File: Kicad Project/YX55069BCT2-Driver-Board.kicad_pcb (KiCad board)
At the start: 6 copper layers, 54.3 x 33.2 mm, 151 parts, among them J1 10029449-001RLF, Q1 BSS138_C112239, Q2 BSS138_C112239, Q4 BSS138_C112239, SW3 BOOT, SW4 RESET, U1 TC358870XBG(NOK), U10 ESP32-S3R8, U11 GD25Q128EWIGR, U12 USBLC6-2SC6, U13 SN74AXC1T45DCKR, U14 TXS0101DBVR, U15 TPS61165DBVR, U16 TVS0500DRVR, U2 TLV76701DRVR, U3 CH224K, U4 TLV76718DRVR, U5 TLV76728DRVR, U6 TLV76733DRVR, U62 PCA9306DCUR, U63 AP2120N-2.8TRG1, U64 PCA9306DCUR, U7 TLV76701DRVR, U8 ESD7104MUTAG_C2987068, U9 TPS259474LRPWR, X1 ABM8-40.000MHZ-10-D1G-T

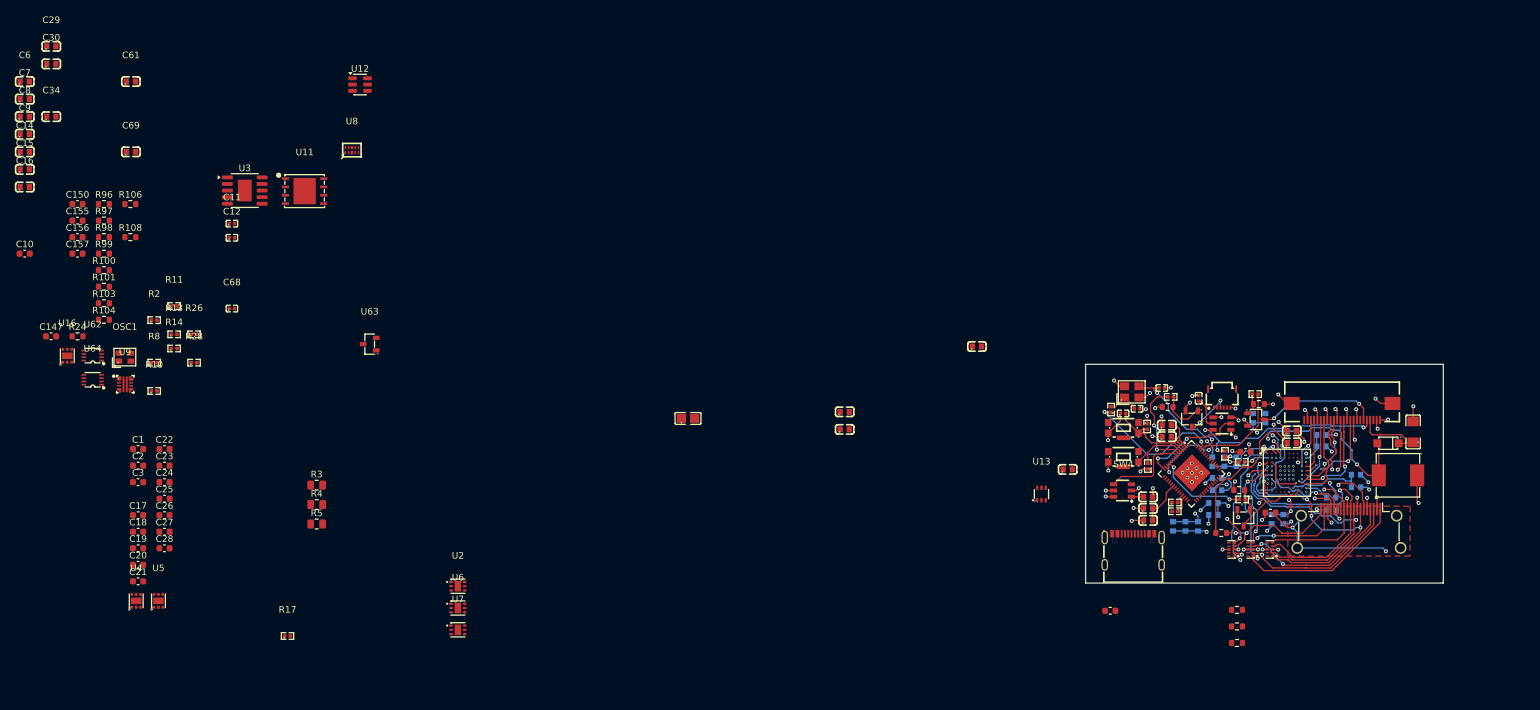
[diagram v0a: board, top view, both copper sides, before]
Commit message: wired up LDOs + USB-C
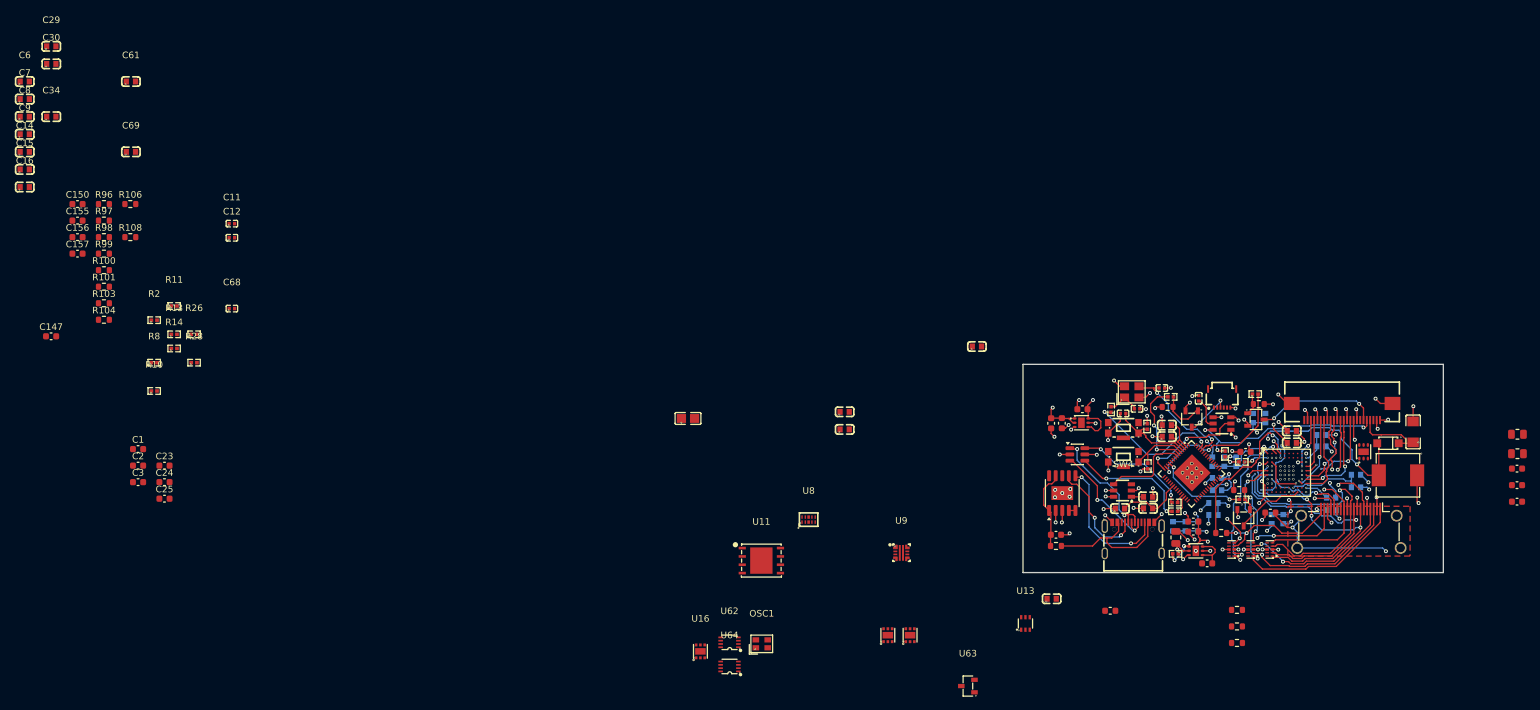
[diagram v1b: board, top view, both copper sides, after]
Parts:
- moved C17 209.5 mm to (163.8, 74.2)
- moved C18 209.5 mm to (163.8, 76.7)
- moved C19 209.5 mm to (163.8, 79.2)
- moved R3 182.5 mm to (163.9, 69.0)
- moved R4 182.5 mm to (163.9, 71.9)
- moved C10 162.3 mm to (93.8, 84.2)
- moved C28 158.3 mm to (116.8, 88.5), turned to 180 degrees
- moved C26 156.2 mm to (114.7, 82.2)
- moved C27 156.2 mm to (114.7, 83.7)
- moved R24 151.9 mm to (93.8, 85.9)
- moved C21 142.3 mm to (94.7, 67.3), turned to 90 degrees
- moved C20 140.3 mm to (93.1, 67.3), turned to 90 degrees
- moved C22 139.5 mm to (97.8, 65.2), turned to 180 degrees
- moved U2 139.0 mm to (140.5, 71.6), turned to 90 degrees
- moved R17 135.4 mm to (111.9, 87.1), turned to 180 degrees
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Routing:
- net GND: track 103.9 -> 126.0 mm, vias 81 -> 102
- net VBUS: track 0.00 -> 21.2 mm
- net CC2: track 0.00 -> 21.0 mm, vias 0 -> 2
- net USB_DN: track 0.00 -> 18.7 mm, vias 0 -> 2
- net USB_DP: track 0.00 -> 18.4 mm, vias 0 -> 2
- net ESP_DP: track 0.00 -> 18.0 mm, vias 0 -> 2
- net ESP_DN: track 0.00 -> 17.6 mm, vias 0 -> 2
- net CC1: track 0.00 -> 16.9 mm, vias 0 -> 2
- net SYS_5V: track 9.35 -> 25.6 mm, vias 3 -> 5
- net VDD: track 0.00 -> 12.2 mm
- net 1V15: track 35.4 -> 46.6 mm, vias 11 -> 14
- net Net-(U7-FB): track 0.00 -> 9.84 mm, vias 0 -> 2
- net 3V3: track 63.7 -> 73.4 mm, vias 11 -> 12
- net Net-(U3-DM): track 0.00 -> 1.00 mm
- added copper zone on In6.Cu, net 1V15
- added copper zone on In5.Cu, net 3V3
- added copper zone on In3.Cu, net GND
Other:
- board size 54.3 x 33.2 mm -> 63.8 x 31.6 mm
- copper layers 6 -> 8

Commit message: wired rest of components, and majority of remaining caps and resistors
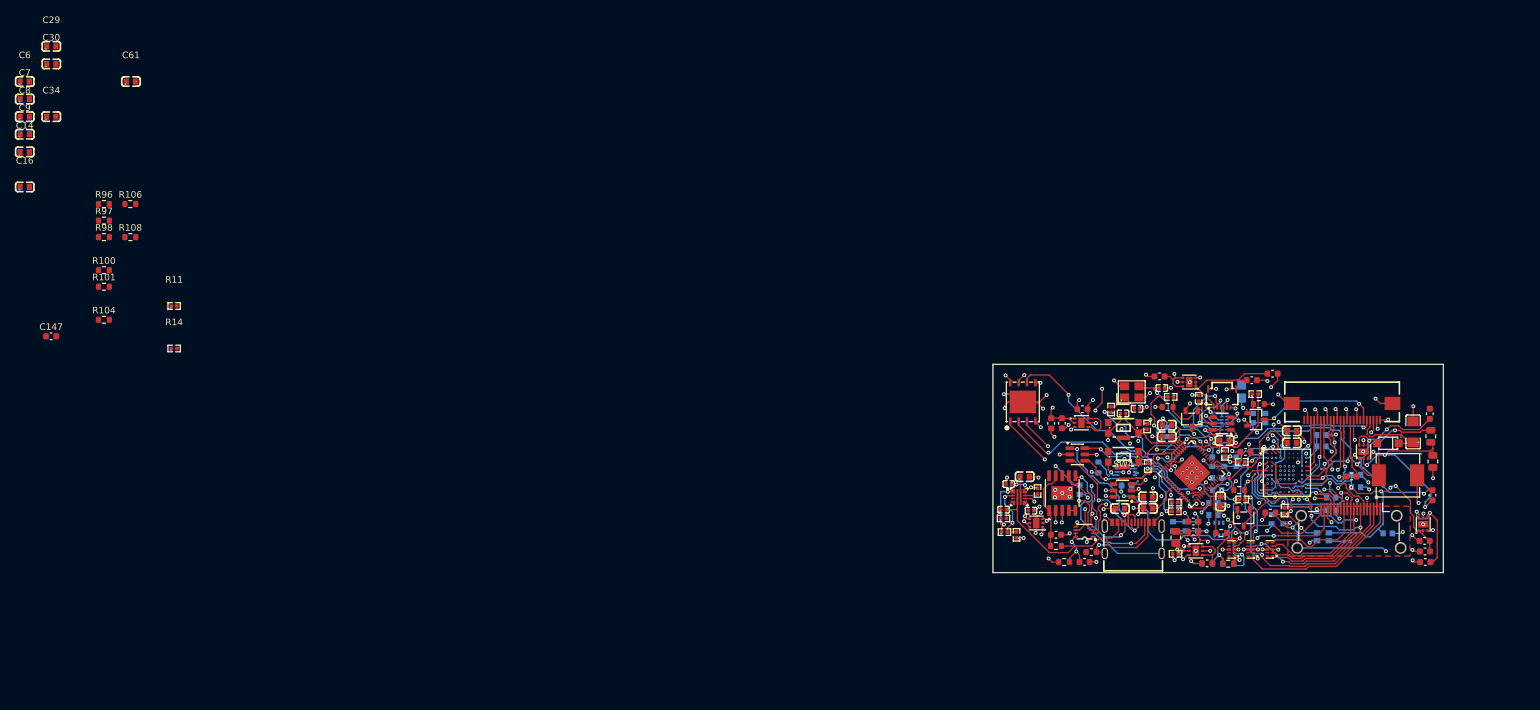
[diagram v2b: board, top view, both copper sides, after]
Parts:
- removed C150, C155: 1µF, Capacitor_SMD:C_0603_1608Metric
- removed U63: AP2120N-2.8TRG1, slate113:SOT-23-3_L2.9-W1.3-P1.90-LS2.4-BR
- C15, C157, C62, C64, C67, OSC1, R103, R19, R2, R20, U13, U64, U8: moved to B.Cu
- moved C15 214.2 mm to (144.2, 84.0), turned to 180 degrees
- moved C23 191.7 mm to (149.8, 85.1)
- moved C24 191.7 mm to (149.8, 86.7)
- moved C25 191.7 mm to (149.9, 88.3), turned to 180 degrees
- moved R2 184.3 mm to (138.0, 85.2)
- moved C3 173.0 mm to (126.7, 59.8), turned to 180 degrees
- moved R13 170.7 mm to (128.5, 80.5), turned to 90 degrees
- moved C2 169.6 mm to (123.5, 60.7), turned to 180 degrees
- moved C157 163.1 mm to (104.5, 76.7), turned to 180 degrees
- moved C156 160.7 mm to (98.1, 88.3)
- moved C1 155.5 mm to (109.5, 60.2), turned to 180 degrees
- moved R99 153.1 mm to (95.0, 88.3), turned to 180 degrees
- moved R103 153.0 mm to (100.2, 74.0), turned to -90 degrees
- moved C69 144.4 mm to (89.0, 75.4)
- moved R8 131.1 mm to (85.8, 81.7)
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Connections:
- C2 pad 2: 2V8 -> TP_2V8
- C3 pad 2: 2V8 -> TP_2V8
- U5 pad 1: 2V8 -> TP_2V8
- U5 pad 2: 2V8 -> TP_2V8
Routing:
- net GND: track 126.0 -> 199.6 mm, vias 102 -> 146
- net TP_SCL_1V8: track 0.00 -> 49.5 mm, vias 0 -> 3
- net SYS_5V: track 25.6 -> 74.5 mm, vias 5 -> 13
- net 1V8: track 14.6 -> 61.7 mm, vias 2 -> 9
- net VDD_SPI: track 0.00 -> 46.9 mm, vias 0 -> 2
- net SPIWP: track 0.00 -> 45.8 mm, vias 0 -> 4
- net SPIHOLD: track 0.00 -> 40.2 mm, vias 0 -> 2
- net SPIQ: track 0.00 -> 40.1 mm, vias 0 -> 2
- net HDMI_SCL: track 0.00 -> 39.7 mm, vias 0 -> 3
- net HDMI_SDA: track 0.00 -> 39.7 mm, vias 0 -> 4
- net TP_SDA_1V8: track 0.00 -> 38.6 mm, vias 0 -> 5
- net SPIDI: track 0.00 -> 37.8 mm, vias 0 -> 2
- net SPICLK: track 0.00 -> 36.5 mm, vias 0 -> 2
- net SPICS0: track 0.00 -> 34.8 mm, vias 0 -> 2
- net I2C0_SDA: track 0.00 -> 33.9 mm, vias 0 -> 4
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- added copper zone on In6.Cu, net 1V8
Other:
- board size 63.8 x 31.6 mm -> 68.4 x 31.6 mm

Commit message: wired up rest of components
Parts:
- C14, C147, C16, C29, C30, C61, C7, C8, C9, R100, R101, R104, R106, R96, R97, R98: moved to B.Cu
- moved C14 208.7 mm to (138.8, 80.0), turned to 180 degrees
- moved C8 206.8 mm to (132.7, 88.2), turned to 180 degrees
- moved C9 200.9 mm to (128.4, 84.9), turned to 90 degrees
- moved R100 190.3 mm to (138.7, 62.3), turned to 180 degrees
- moved C147 189.2 mm to (130.2, 62.1)
- moved R96 187.8 mm to (134.9, 62.2), turned to 180 degrees
- moved C29 183.4 mm to (107.2, 88.2)
- moved C16 178.7 mm to (107.3, 86.0)
- moved R11 170.1 mm to (126.8, 82.3)
- moved R14 162.7 mm to (121.5, 74.4)
- moved C30 160.8 mm to (91.3, 70.4), turned to 90 degrees
- moved C6 160.1 mm to (87.4, 70.9)
- moved C7 159.3 mm to (89.1, 66.1), turned to 180 degrees
- moved R104 157.3 mm to (104.1, 79.2), turned to -90 degrees
- moved C34 155.2 mm to (87.4, 72.8)
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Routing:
- net 1V8: track 61.7 -> 119.0 mm, vias 9 -> 17
- net HDMI_INT: track 0.00 -> 30.4 mm, vias 0 -> 2
- net 3V3: track 97.0 -> 126.0 mm, vias 20 -> 27
- net INT: track 0.00 -> 28.9 mm, vias 0 -> 4
- net TP_RST_L: track 11.4 -> 37.4 mm
- net GND: track 199.6 -> 222.0 mm, vias 146 -> 156
- net Net-(U1-BIASDA): track 0.00 -> 20.2 mm, vias 0 -> 3
- net Net-(U1-PCKIN): track 0.00 -> 18.1 mm, vias 0 -> 3
- net Net-(U1-PFIL): track 0.00 -> 17.4 mm, vias 0 -> 2
- net SYS_5V: track 74.5 -> 87.2 mm
- net VDD_SPI: track 46.9 -> 57.5 mm
- net 1V15: track 46.8 -> 56.9 mm, vias 14 -> 16
- net TP_SDA_1V8: track 38.6 -> 48.7 mm, vias 5 -> 6
- net HDMI_SCL: track 39.7 -> 48.5 mm, vias 3 -> 6
- net Net-(Q1-D): track 10.5 -> 16.2 mm
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
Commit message: fixed most of DRC errors
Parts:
- moved C45 0.06 mm to (118.2, 75.5)
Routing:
- net 1V2: track 45.9 -> 63.2 mm, vias 7 -> 8
- net GND: track 222.0 -> 239.2 mm, vias 156 -> 163
- net 1V8: track 119.0 -> 130.2 mm, vias 17 -> 20
- net SYS_5V: track 87.2 -> 89.5 mm, vias 13 -> 15
- net HDMICP: track 44.0 -> 43.0 mm
- net HDMI_SDA: track 41.8 -> 42.6 mm
- net HDMICN: track 32.7 -> 32.0 mm
- net Net-(U1-BIASDA): track 20.2 -> 20.7 mm
- net HDMI_5V_IN: track 56.4 -> 56.9 mm
- net D0+: track 43.8 -> 43.3 mm
- net 3V3: track 126.0 -> 126.3 mm, vias 27 -> 28

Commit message: fixed remaining DRC issues
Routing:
- net 1V15: track 56.7 -> 65.7 mm, vias 16 -> 17
- net GND: track 239.2 -> 238.7 mm

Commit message: add README + production files
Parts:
- J1: value 10029449-001RLF -> 10029449-111RLF
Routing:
- net VDD_SPI: track 57.5 -> 52.9 mm
- net 3V3: track 126.0 -> 128.1 mm
- net SPIHOLD: track 40.0 -> 40.7 mm
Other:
- board text added: "."
- board text added: "Hack Club"
- board text added: "YX55069BCT2"
- board text added: "xeno3dev .3"
- board text added: "|"
